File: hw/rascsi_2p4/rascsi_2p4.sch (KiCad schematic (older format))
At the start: 91 parts, among them J1 Raspberry_Pi_2_3, J2 DNP, J4 I2C Pinout, J5 DNP, J6 CONNFLY DB-25, J7 DNP, U1 74ALVC164245DGG, U2 74ALVC164245DGG, U3 UCC5606PWPTR, U4 UCC5606PWPTR, U5 NarrowPowerAdapter, U6 NarrowPowerAdapter, X1 Mac, X3 Mac, X7 Pi, X8 Pi

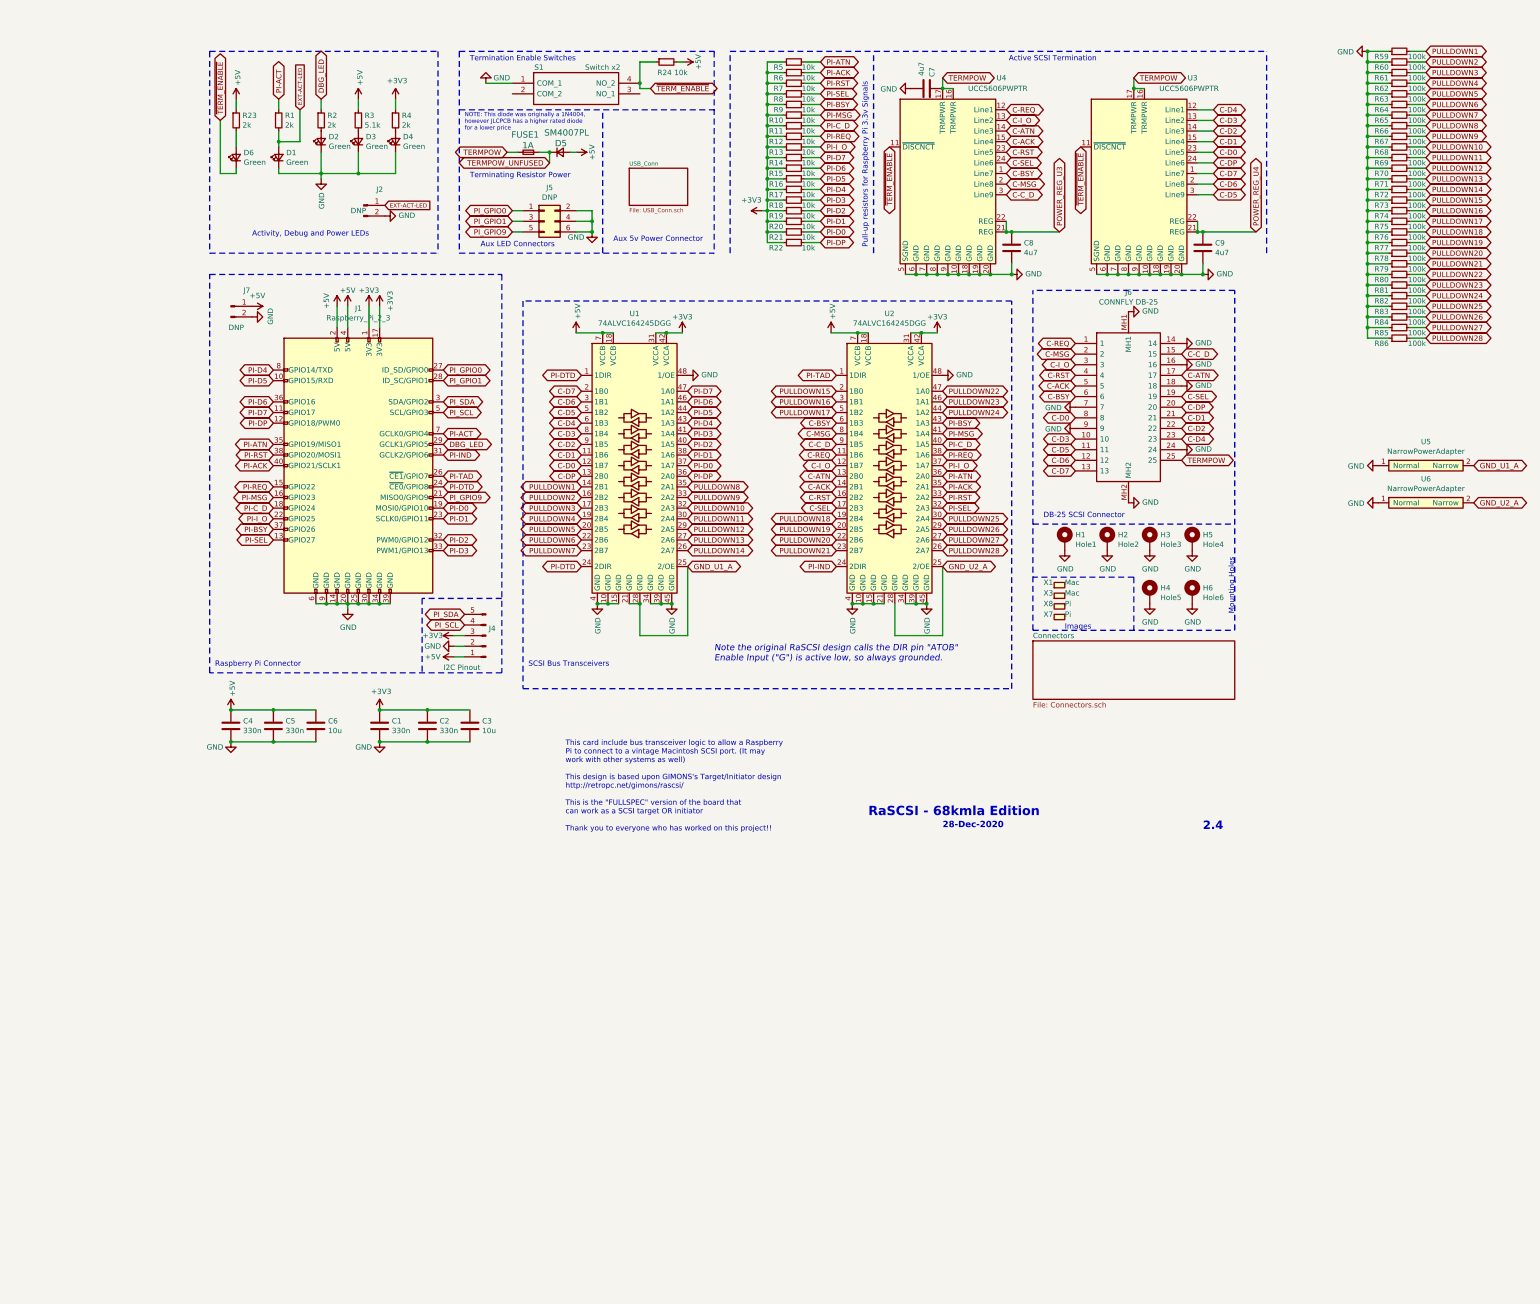
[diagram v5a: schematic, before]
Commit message: first routable version
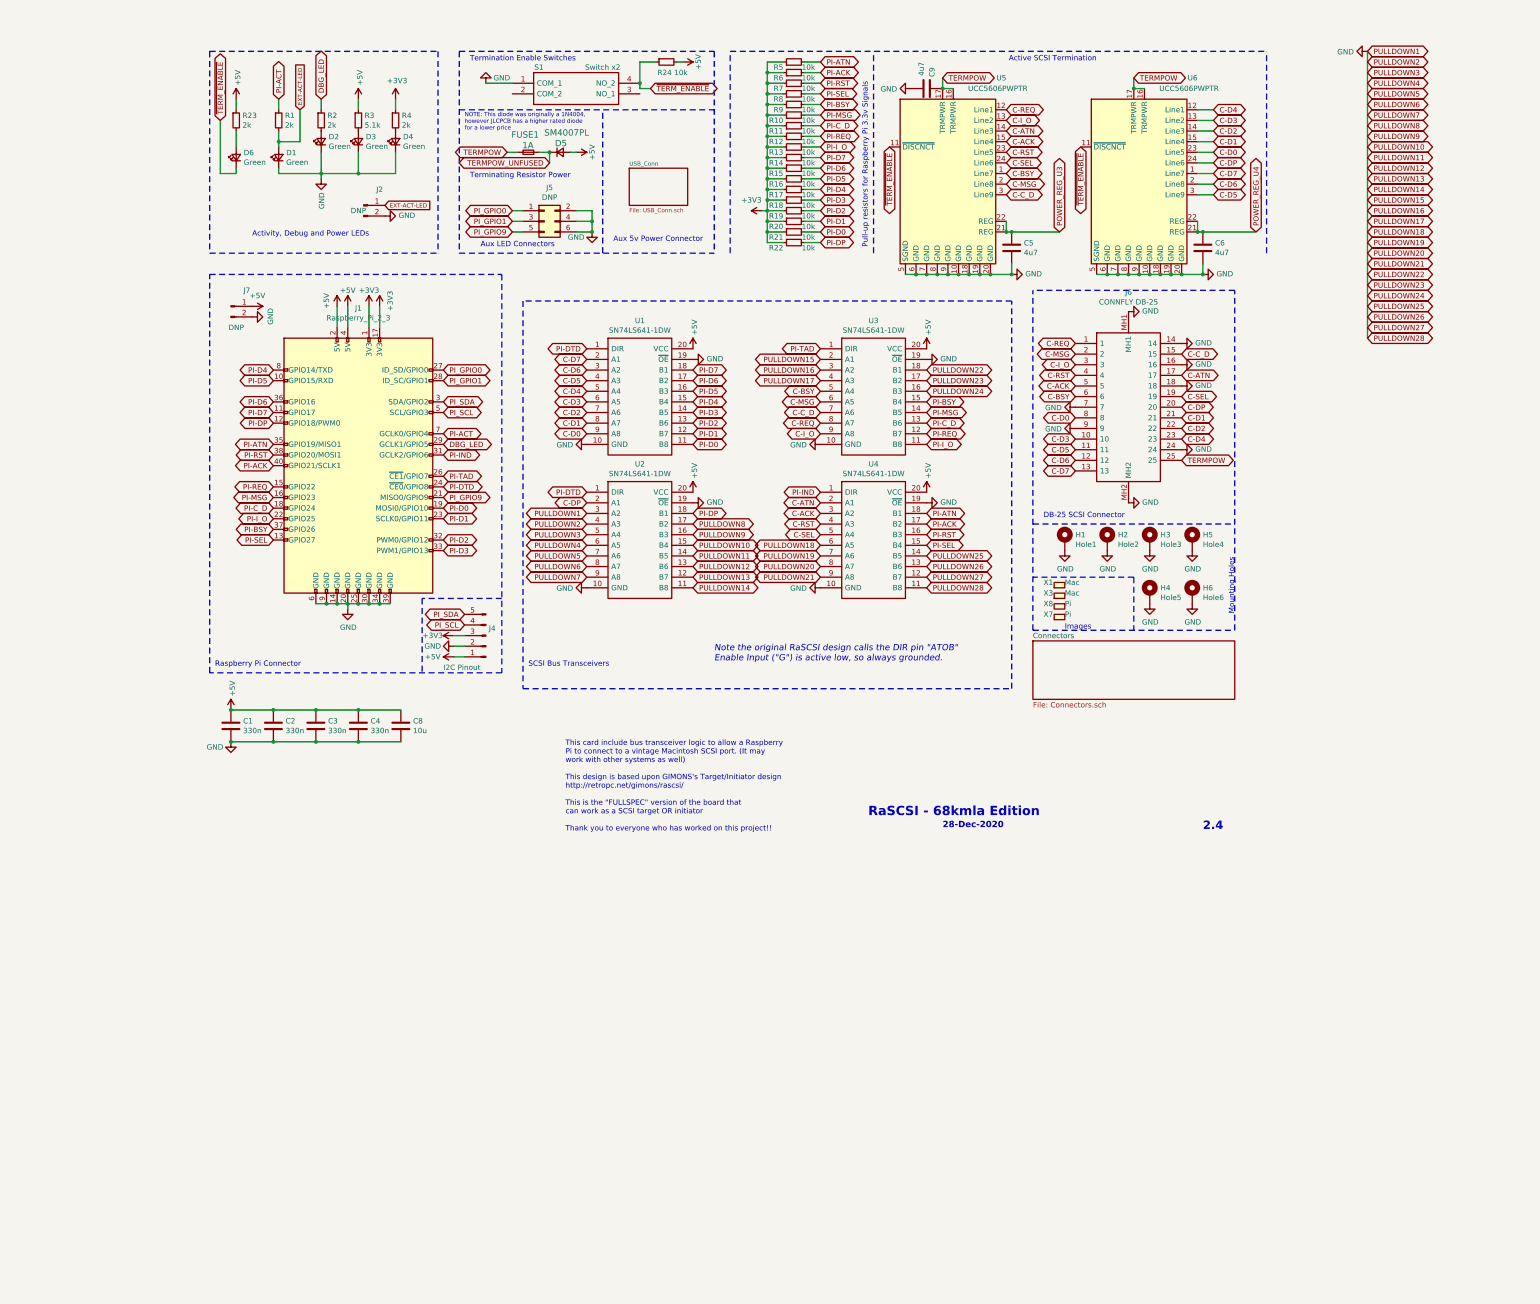
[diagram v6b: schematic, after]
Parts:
- removed C3: 10u, Capacitor_SMD:C_0805_2012Metric, symbol Device:C
- removed R59, R60, R61, R62, R63, R64, R65, R66, R67, R68, R69, R70, R71, R72, R73, R74, R75, R76, R77, R78, R79, R80, R81, R82, R83, R84, R85, R86: 100k, Resistor_SMD:R_0402_1005Metric, symbol Device:R_Small
- removed U1, U2: 74ALVC164245DGG, Package_SO:TSSOP-48_6.1x12.5mm_P0.5mm, symbol amiga:74ALVC164245DGG
- removed U5, U6: NarrowPowerAdapter, amiga:NarrowPowerAdapter_0.60_to_0.25, symbol amiga:NarrowPowerAdapter
- added U1, U2, U3, U4: SN74LS641-1DW, Package_SO:SOIC-20W_7.5x12.8mm_P1.27mm, symbol SamacSys_Parts:SN74LS245DW
- renumbered C4 to C3, C5 to C4, C8 to C5, C9 to C6, C6 to C8, C7 to C9, U4 to U5, U3 to U6
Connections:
- net +3V3: no longer C1.1, C2.1
- net +5V: now also C1.1, C2.1, U1.20 (VCC), U2.20 (VCC), U3.20 (VCC), U4.20 (VCC)
- net C-ACK: now also U4.3 (A2)
- net C-ATN: now also U4.2 (A1)
- net C-BSY: now also U3.5 (A4)
- net C-C_D: now also U3.7 (A6)
- net C-D0: now also U1.9 (A8)
- net C-D1: now also U1.8 (A7)
- net C-D2: now also U1.7 (A6)
- net C-D3: now also U1.6 (A5)
- net C-D4: now also U1.5 (A4)
- net C-D5: now also U1.4 (A3)
- net C-D6: now also U1.3 (A2)
- net C-D7: now also U1.2 (A1)
- net C-DP: now also U2.2 (A1)
- net C-I_O: now also U3.9 (A8)
- net C-MSG: now also U3.6 (A5)
- net C-REQ: now also U3.8 (A7)
- net C-RST: now also U4.4 (A3)
- net C-SEL: now also U4.5 (A4)
- net GND: now also U1.10 (GND), U1.19 (~OE), U2.10 (GND), U2.11 (B8), U2.12 (B7), U2.13 (B6), U2.14 (B5), U2.15 (B4), U2.16 (B3), U2.17 (B2), U2.19 (~OE), U2.3 (A2), U2.4 (A3), U2.5 (A4), U2.6 (A5), U2.7 (A6), U2.8 (A7), U2.9 (A8), U3.10 (GND), U3.16 (B3), U3.17 (B2), U3.18 (B1), U3.19 (~OE), U3.2 (A1), U3.3 (A2), U3.4 (A3), U4.10 (GND), U4.11 (B8), U4.12 (B7), U4.13 (B6), U4.14 (B5), U4.19 (~OE), U4.6 (A5), U4.7 (A6), U4.8 (A7), U4.9 (A8)
- net PI-ACK: now also U4.17 (B2)
- net PI-ATN: now also U4.18 (B1)
- net PI-BSY: now also U3.15 (B4)
- net PI-C_D: now also U3.13 (B6)
- net PI-D0: now also U1.11 (B8)
- net PI-D1: now also U1.12 (B7)
- net PI-D2: now also U1.13 (B6)
- net PI-D3: now also U1.14 (B5)
- net PI-D4: now also U1.15 (B4)
- net PI-D5: now also U1.16 (B3)
- net PI-D6: now also U1.17 (B2)
- net PI-D7: now also U1.18 (B1)
- net PI-DP: now also U2.18 (B1)
- net PI-DTD: now also U1.1 (DIR), U2.1 (DIR)
- net PI-IND: now also U4.1 (DIR)
- net PI-I_O: now also U3.11 (B8)
- net PI-MSG: now also U3.14 (B5)
- net PI-REQ: now also U3.12 (B7)
- net PI-RST: now also U4.16 (B3)
- net PI-SEL: now also U4.15 (B4)
- net PI-TAD: now also U3.1 (DIR)
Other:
- moved on the sheet: C3, C4, C8

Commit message: moved components to make space for 50 pin conn
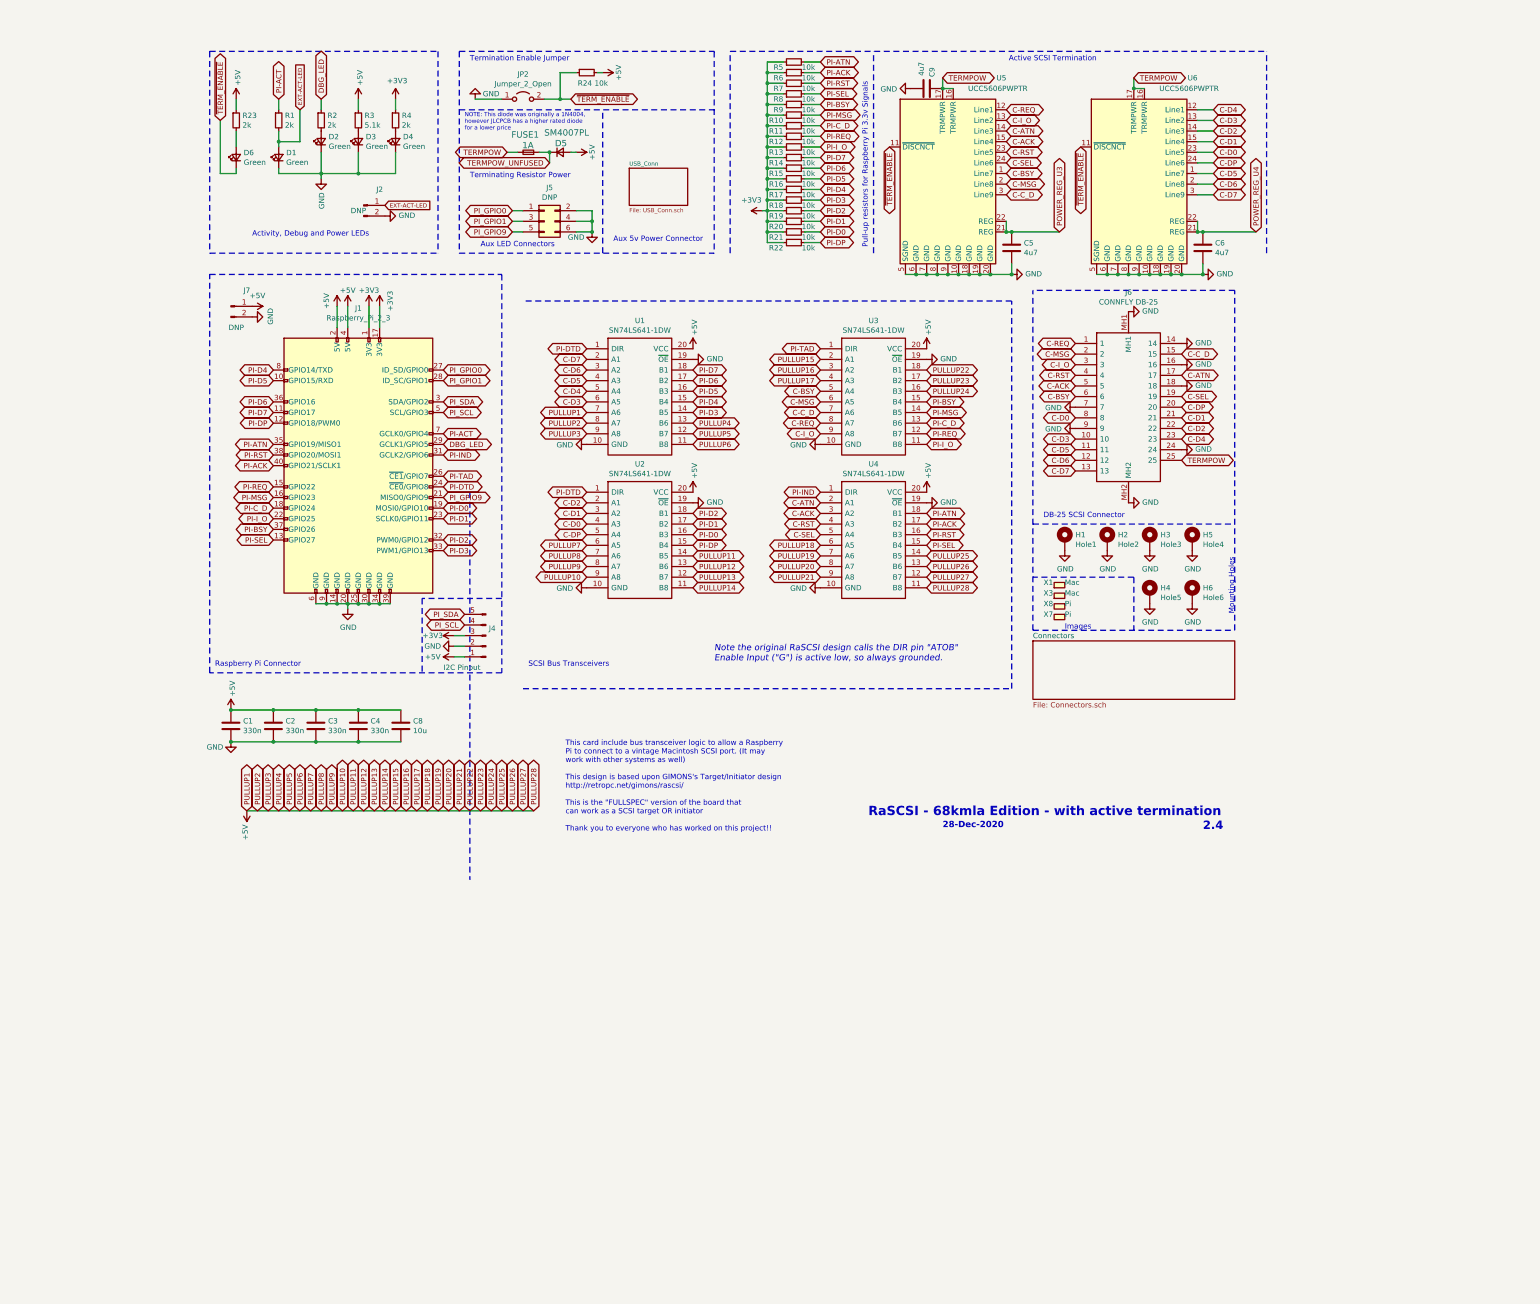
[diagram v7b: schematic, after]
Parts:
- removed S1: Switch x2, rascsi_din:SOIC127P812X230-4N, symbol SamacSys_Parts:TDA02H0SB1R
- added JP2: Jumper_2_Open, Connector_PinHeader_2.54mm:PinHeader_1x02_P2.54mm_Horizontal, symbol Jumper:Jumper_2_Open
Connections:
- net +5V: now also U1.11 (B8), U1.12 (B7), U1.13 (B6), U1.7 (A6), U1.8 (A7), U1.9 (A8), U2.11 (B8), U2.12 (B7), U2.13 (B6), U2.14 (B5), U2.6 (A5), U2.7 (A6), U2.8 (A7), U2.9 (A8), U3.16 (B3), U3.17 (B2), U3.18 (B1), U3.2 (A1), U3.3 (A2), U3.4 (A3), U4.11 (B8), U4.12 (B7), U4.13 (B6), U4.14 (B5), U4.6 (A5), U4.7 (A6), U4.8 (A7), U4.9 (A8)
- net C-D0: now also U2.4 (A3); no longer U1.9 (A8)
- net C-D1: now also U2.3 (A2); no longer U1.8 (A7)
- net C-D2: now also U2.2 (A1); no longer U1.7 (A6)
- net C-D5: now also U6.1 (Line7); no longer U6.3 (Line9)
- net C-D7: now also U6.3 (Line9); no longer U6.1 (Line7)
- net C-DP: now also U2.5 (A4); no longer U2.2 (A1)
- net GND: now also JP2.1 (A); no longer U2.11 (B8), U2.12 (B7), U2.13 (B6), U2.14 (B5), U2.15 (B4), U2.16 (B3), U2.17 (B2), U2.3 (A2), U2.4 (A3), U2.5 (A4), U2.6 (A5), U2.7 (A6), U2.8 (A7), U2.9 (A8), U3.16 (B3), U3.17 (B2), U3.18 (B1), U3.2 (A1), U3.3 (A2), U3.4 (A3), U4.11 (B8), U4.12 (B7), U4.13 (B6), U4.14 (B5), U4.6 (A5), U4.7 (A6), U4.8 (A7), U4.9 (A8)
- net PI-D0: now also U2.16 (B3); no longer U1.11 (B8)
- net PI-D1: now also U2.17 (B2); no longer U1.12 (B7)
- net PI-D2: now also U2.18 (B1); no longer U1.13 (B6)
- net PI-DP: now also U2.15 (B4); no longer U2.18 (B1)
- net ~TERM_ENABLE: now also JP2.2 (B)
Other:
- note added: "RaSCSI - 68kmla Edition - with active termination"
- note added: "Termination Enable Jumper"
- note removed: "RaSCSI - 68kmla Edition"
- note removed: "Termination Enable Switches"
- moved on the sheet: R24

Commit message: optimized routing (81 vias)
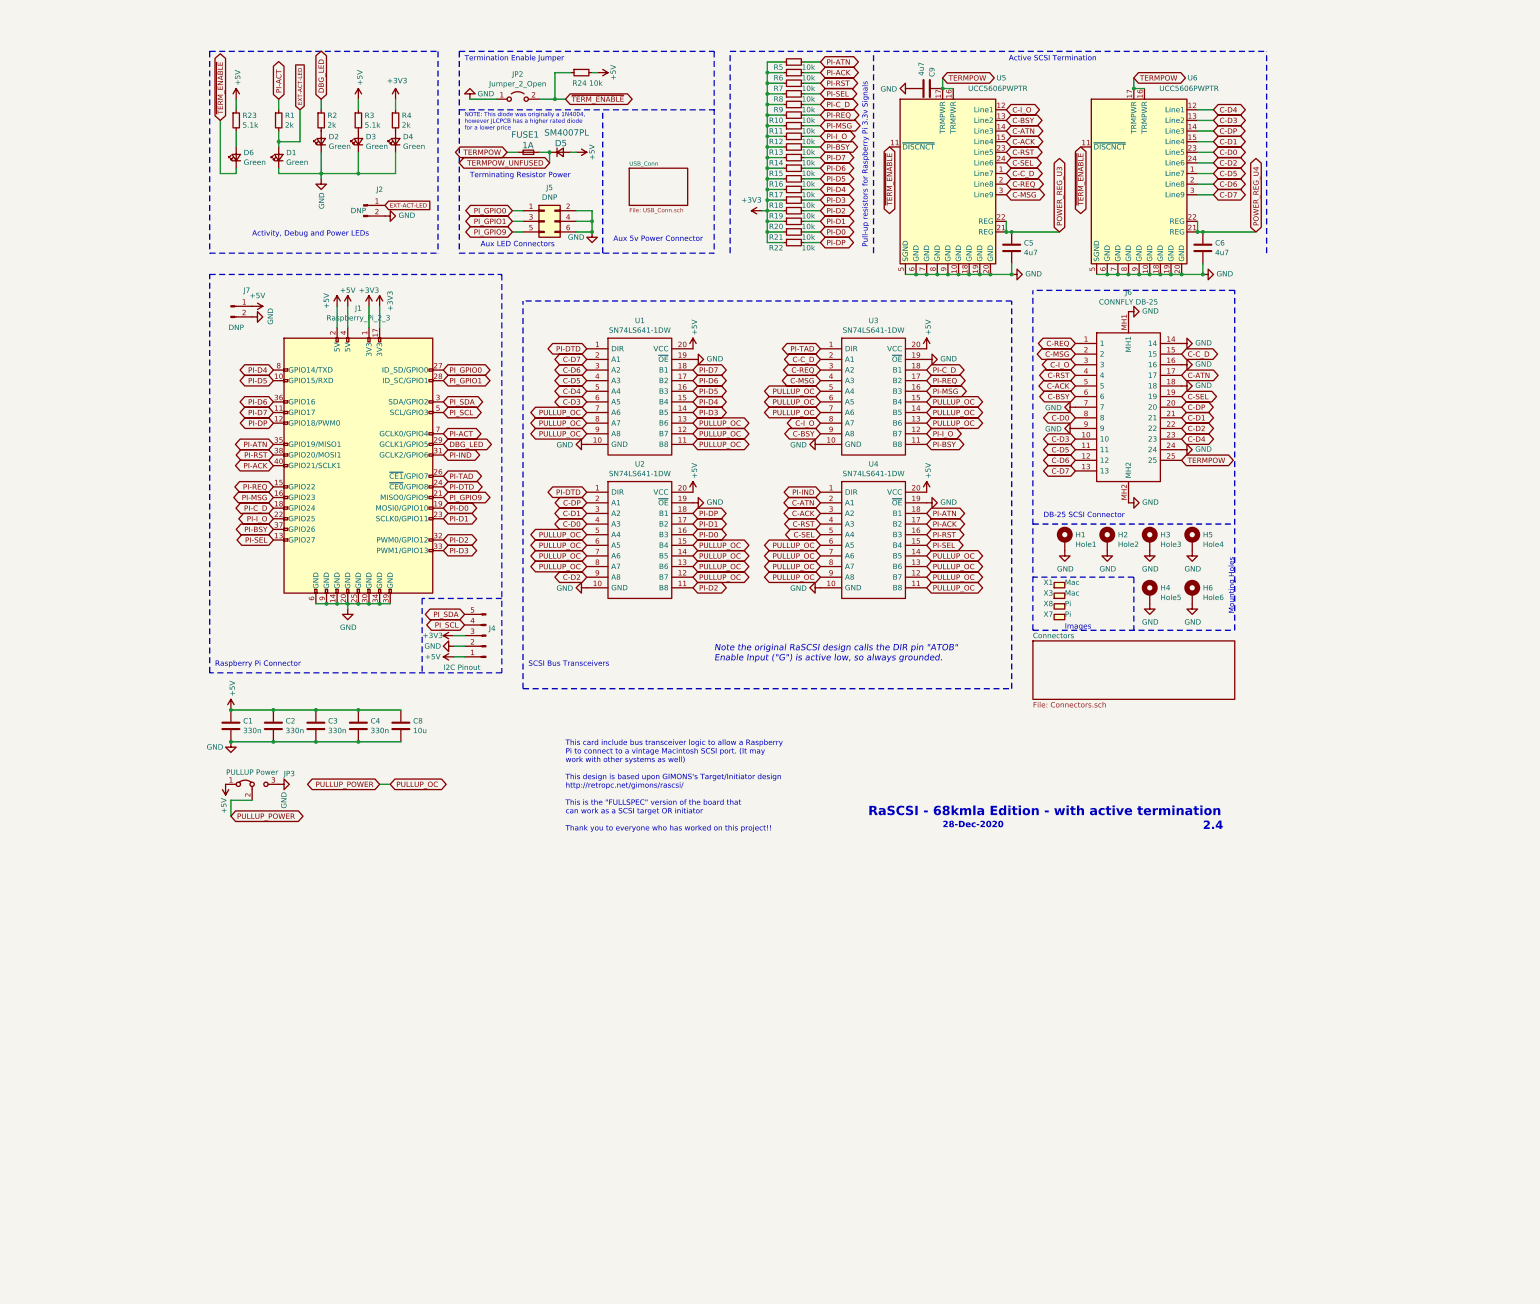
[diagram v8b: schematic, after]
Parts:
- added JP3: PULLUP Power, Jumper:SolderJumper-3_P1.3mm_Bridged12_RoundedPad1.0x1.5mm, symbol Jumper:Jumper_3_Bridged12
- R23: value 2k -> 5.1k; Description 2kΩ ±1% 1/16W ±100ppm/℃ 0402 Chip Resistor -> 5.1kΩ ±1% 1/16W ±100ppm/℃ 0402 Chip Resistor; LCSC C4109 -> C25905; Manufacturer_Part_Number 0402WGF2001TCE -> 0402WGF5101TCE
- U1, U2, U3, U4: LCSC (none) -> C1548111; Manufacturer_Part_Number SN74LS245DW -> SN74LS641-1DW
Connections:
- net +5V: now also JP3.1 (A); no longer U1.11 (B8), U1.12 (B7), U1.13 (B6), U1.7 (A6), U1.8 (A7), U1.9 (A8), U2.11 (B8), U2.12 (B7), U2.13 (B6), U2.14 (B5), U2.6 (A5), U2.7 (A6), U2.8 (A7), U2.9 (A8), U3.16 (B3), U3.17 (B2), U3.18 (B1), U3.2 (A1), U3.3 (A2), U3.4 (A3), U4.11 (B8), U4.12 (B7), U4.13 (B6), U4.14 (B5), U4.6 (A5), U4.7 (A6), U4.8 (A7), U4.9 (A8)
- net C-BSY: now also U3.9 (A8), U5.13 (Line2); no longer U3.5 (A4), U5.1 (Line7)
- net C-C_D: now also U3.2 (A1), U5.1 (Line7); no longer U3.7 (A6), U5.3 (Line9)
- net C-D2: now also U2.9 (A8), U6.24 (Line6); no longer U2.2 (A1), U6.14 (Line3)
- net C-DP: now also U2.2 (A1), U6.14 (Line3); no longer U2.5 (A4), U6.24 (Line6)
- net C-I_O: now also U3.8 (A7), U5.12 (Line1); no longer U3.9 (A8), U5.13 (Line2)
- net C-MSG: now also U3.4 (A3), U5.3 (Line9); no longer U3.6 (A5), U5.2 (Line8)
- net C-REQ: now also U3.3 (A2), U5.2 (Line8); no longer U3.8 (A7), U5.12 (Line1)
- net GND: now also JP3.3 (B)
- net PI-BSY: now also R13.2, U3.11 (B8); no longer R9.2, U3.15 (B4)
- net PI-C_D: now also R9.2, U3.18 (B1); no longer R11.2, U3.13 (B6)
- net PI-D2: now also U2.11 (B8); no longer U2.18 (B1)
- net PI-DP: now also U2.18 (B1); no longer U2.15 (B4)
- net PI-I_O: now also R12.2, U3.12 (B7); no longer R13.2, U3.11 (B8)
- net PI-MSG: now also R11.2, U3.16 (B3); no longer R10.2, U3.14 (B5)
- net PI-REQ: now also R10.2, U3.17 (B2); no longer R12.2, U3.12 (B7)
- new net PULLUP_OC: JP3.2 (C), U1.11 (B8), U1.12 (B7), U1.13 (B6), U1.7 (A6), U1.8 (A7), U1.9 (A8), U2.12 (B7), U2.13 (B6), U2.14 (B5), U2.15 (B4), U2.5 (A4), U2.6 (A5), U2.7 (A6), U2.8 (A7), U3.13 (B6), U3.14 (B5), U3.15 (B4), U3.5 (A4), U3.6 (A5), U3.7 (A6), U4.11 (B8), U4.12 (B7), U4.13 (B6), U4.14 (B5), U4.6 (A5), U4.7 (A6), U4.8 (A7), U4.9 (A8)
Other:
- moved on the sheet: JP2, R24
